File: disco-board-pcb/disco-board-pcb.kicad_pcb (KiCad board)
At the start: 2 copper layers, 57.2 x 82.6 mm, 6 parts, among them J101 Conn_02x32_Odd_Even, J102 Conn_02x32_Odd_Even, U101 MMA8653FCR1

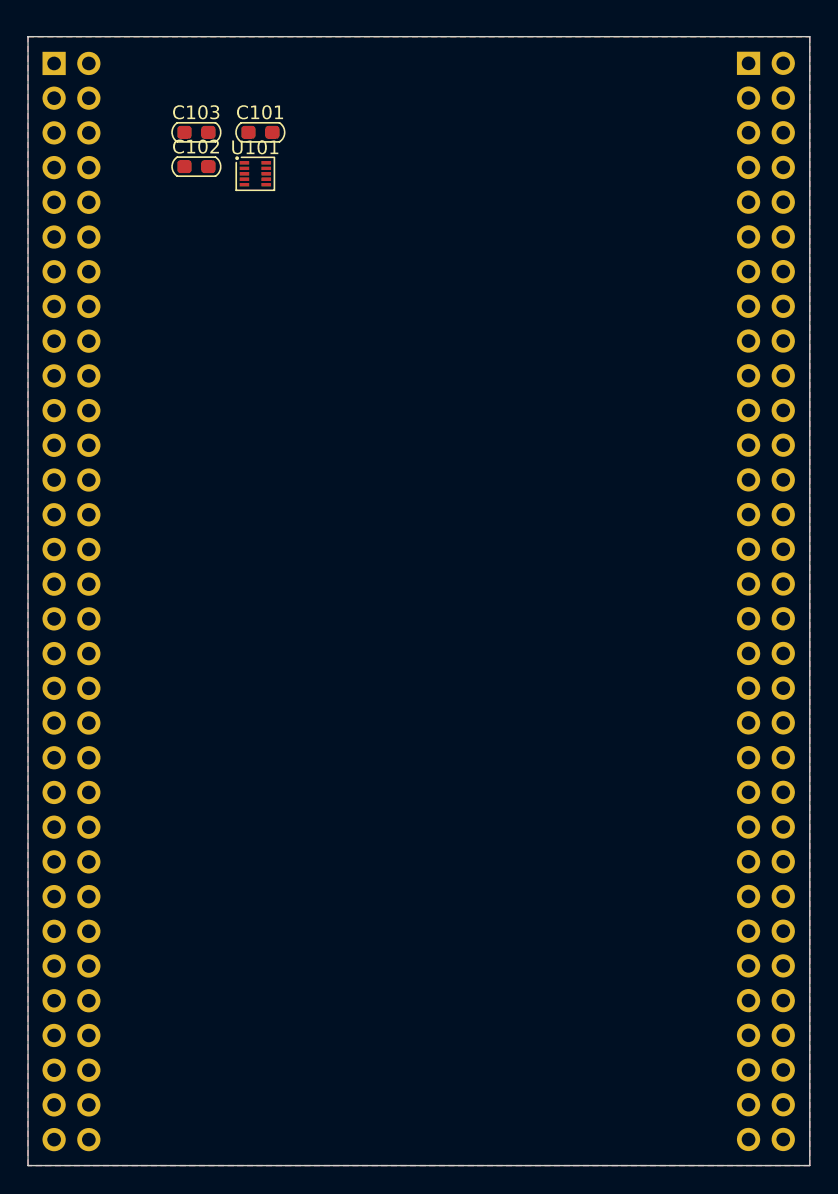
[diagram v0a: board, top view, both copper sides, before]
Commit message: Completing schematic and putting test points on PCB
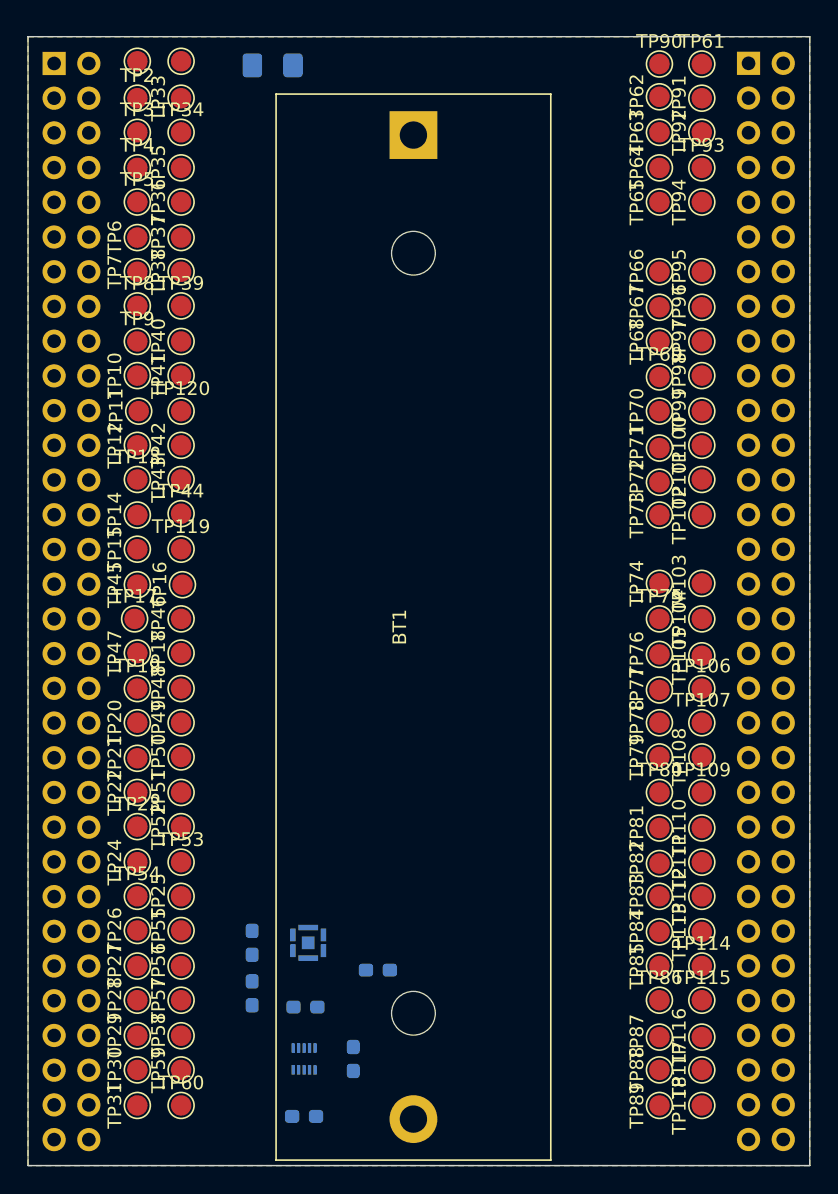
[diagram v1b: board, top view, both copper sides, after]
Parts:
- added BT1: Battery_Cell, Battery:BatteryHolder_MPD_BH-18650-PC2, F.Cu at (130.4, 65.8)
- added C2: LPS28DFWTR, local:LPS28DFWTR, B.Cu at (122.7, 124.9)
- added C5: 100nF, Capacitor_SMD_AKL:C_0603_1608Metric_Pad1.05x0.95mm, B.Cu at (127.8, 126.9)
- added F1: FUSE_SMD, Fuse_AKL:Fuse_1206_3216Metric_Pad1.42x1.75mm_BigPads, B.Cu at (120.1, 60.7)
- added R1: 10k, Resistor_SMD_AKL:R_0603_1608Metric_Pad1.05x0.95mm, B.Cu at (118.6, 124.9)
- added R2: 10k, Resistor_SMD_AKL:R_0603_1608Metric_Pad1.05x0.95mm, B.Cu at (118.6, 128.6)
- added TP1: TestPoint, TestPoint:TestPoint_Pad_D1.5mm, F.Cu at (110.2, 60.4)
- added TP10: TestPoint, TestPoint:TestPoint_Pad_D1.5mm, F.Cu at (110.2, 83.4)
- added TP100: TestPoint, TestPoint:TestPoint_Pad_D1.5mm, F.Cu at (151.5, 88.5)
- added TP101: TestPoint, TestPoint:TestPoint_Pad_D1.5mm, F.Cu at (151.5, 91.0)
- added TP102: TestPoint, TestPoint:TestPoint_Pad_D1.5mm, F.Cu at (151.5, 93.6)
- added TP103: TestPoint, TestPoint:TestPoint_Pad_D1.5mm, F.Cu at (151.5, 98.6)
- added TP104: TestPoint, TestPoint:TestPoint_Pad_D1.5mm, F.Cu at (151.5, 101.2)
- added TP105: TestPoint, TestPoint:TestPoint_Pad_D1.5mm, F.Cu at (151.5, 103.9)
- added TP106: TestPoint, TestPoint:TestPoint_Pad_D1.5mm, F.Cu at (151.5, 106.3)
- added TP107: TestPoint, TestPoint:TestPoint_Pad_D1.5mm, F.Cu at (151.5, 108.8)
- added TP108: TestPoint, TestPoint:TestPoint_Pad_D1.5mm, F.Cu at (151.5, 111.3)
- added TP109: TestPoint, TestPoint:TestPoint_Pad_D1.5mm, F.Cu at (151.5, 113.9)
- added TP11: TestPoint, TestPoint:TestPoint_Pad_D1.5mm, F.Cu at (110.3, 86.0)
- added TP110: TestPoint, TestPoint:TestPoint_Pad_D1.5mm, F.Cu at (151.5, 116.5)
- added TP111: TestPoint, TestPoint:TestPoint_Pad_D1.5mm, F.Cu at (151.5, 119.0)
- added TP112: TestPoint, TestPoint:TestPoint_Pad_D1.5mm, F.Cu at (151.5, 121.5)
- added TP113: TestPoint, TestPoint:TestPoint_Pad_D1.5mm, F.Cu at (151.5, 124.1)
- added TP114: TestPoint, TestPoint:TestPoint_Pad_D1.5mm, F.Cu at (151.5, 126.6)
- added TP115: TestPoint, TestPoint:TestPoint_Pad_D1.5mm, F.Cu at (151.5, 129.1)
- added TP116: TestPoint, TestPoint:TestPoint_Pad_D1.5mm, F.Cu at (151.5, 131.8)
- added TP117: TestPoint, TestPoint:TestPoint_Pad_D1.5mm, F.Cu at (151.5, 134.2)
- added TP118: TestPoint, TestPoint:TestPoint_Pad_D1.5mm, F.Cu at (151.5, 136.8)
- added TP119: TestPoint, TestPoint:TestPoint_Pad_D1.5mm, F.Cu at (113.4, 96.1)
- added TP12: TestPoint, TestPoint:TestPoint_Pad_D1.5mm, F.Cu at (110.2, 88.5)
- added TP120: TestPoint, TestPoint:TestPoint_Pad_D1.5mm, F.Cu at (113.4, 86.0)
- added TP13: TestPoint, TestPoint:TestPoint_Pad_D1.5mm, F.Cu at (110.2, 91.0)
- added TP14: TestPoint, TestPoint:TestPoint_Pad_D1.5mm, F.Cu at (110.2, 93.6)
- added TP15: TestPoint, TestPoint:TestPoint_Pad_D1.5mm, F.Cu at (110.2, 96.1)
- added TP16: TestPoint, TestPoint:TestPoint_Pad_D1.5mm, F.Cu at (113.5, 98.7)
- added TP17: TestPoint, TestPoint:TestPoint_Pad_D1.5mm, F.Cu at (110.0, 101.2)
- added TP18: TestPoint, TestPoint:TestPoint_Pad_D1.5mm, F.Cu at (113.4, 103.7)
- added TP19: TestPoint, TestPoint:TestPoint_Pad_D1.5mm, F.Cu at (110.2, 106.3)
- added TP2: TestPoint, TestPoint:TestPoint_Pad_D1.5mm, F.Cu at (110.2, 63.1)
- added TP20: TestPoint, TestPoint:TestPoint_Pad_D1.5mm, F.Cu at (110.2, 108.8)
- added TP21: TestPoint, TestPoint:TestPoint_Pad_D1.5mm, F.Cu at (110.2, 111.4)
- added TP22: TestPoint, TestPoint:TestPoint_Pad_D1.5mm, F.Cu at (110.2, 113.9)
- added TP23: TestPoint, TestPoint:TestPoint_Pad_D1.5mm, F.Cu at (110.2, 116.4)
- added TP24: TestPoint, TestPoint:TestPoint_Pad_D1.5mm, F.Cu at (110.2, 119.0)
- added TP25: TestPoint, TestPoint:TestPoint_Pad_D1.5mm, F.Cu at (113.4, 121.5)
- added TP26: TestPoint, TestPoint:TestPoint_Pad_D1.5mm, F.Cu at (110.2, 124.0)
- added TP27: TestPoint, TestPoint:TestPoint_Pad_D1.5mm, F.Cu at (110.2, 126.6)
- added TP28: TestPoint, TestPoint:TestPoint_Pad_D1.5mm, F.Cu at (110.2, 129.1)
- added TP29: TestPoint, TestPoint:TestPoint_Pad_D1.5mm, F.Cu at (110.2, 131.7)
- added TP3: TestPoint, TestPoint:TestPoint_Pad_D1.5mm, F.Cu at (110.2, 65.6)
- added TP30: TestPoint, TestPoint:TestPoint_Pad_D1.5mm, F.Cu at (110.2, 134.2)
- added TP31: TestPoint, TestPoint:TestPoint_Pad_D1.5mm, F.Cu at (110.2, 136.8)
- added TP32: TestPoint, TestPoint:TestPoint_Pad_D1.5mm, F.Cu at (113.4, 60.4)
- added TP33: TestPoint, TestPoint:TestPoint_Pad_D1.5mm, F.Cu at (113.4, 63.1)
- added TP34: TestPoint, TestPoint:TestPoint_Pad_D1.5mm, F.Cu at (113.4, 65.6)
- added TP35: TestPoint, TestPoint:TestPoint_Pad_D1.5mm, F.Cu at (113.4, 68.2)
- added TP36: TestPoint, TestPoint:TestPoint_Pad_D1.5mm, F.Cu at (113.4, 70.7)
- added TP37: TestPoint, TestPoint:TestPoint_Pad_D1.5mm, F.Cu at (113.4, 73.3)
- added TP38: TestPoint, TestPoint:TestPoint_Pad_D1.5mm, F.Cu at (113.4, 75.8)
- added TP39: TestPoint, TestPoint:TestPoint_Pad_D1.5mm, F.Cu at (113.4, 78.3)
- added TP4: TestPoint, TestPoint:TestPoint_Pad_D1.5mm, F.Cu at (110.2, 68.2)
- added TP40: TestPoint, TestPoint:TestPoint_Pad_D1.5mm, F.Cu at (113.4, 80.9)
- added TP41: TestPoint, TestPoint:TestPoint_Pad_D1.5mm, F.Cu at (113.4, 83.4)
- added TP42: TestPoint, TestPoint:TestPoint_Pad_D1.5mm, F.Cu at (113.4, 88.5)
- added TP43: TestPoint, TestPoint:TestPoint_Pad_D1.5mm, F.Cu at (113.4, 91.0)
- added TP44: TestPoint, TestPoint:TestPoint_Pad_D1.5mm, F.Cu at (113.4, 93.5)
- added TP45: TestPoint, TestPoint:TestPoint_Pad_D1.5mm, F.Cu at (110.2, 98.7)
- added TP46: TestPoint, TestPoint:TestPoint_Pad_D1.5mm, F.Cu at (113.4, 101.2)
- added TP47: TestPoint, TestPoint:TestPoint_Pad_D1.5mm, F.Cu at (110.2, 103.7)
- added TP48: TestPoint, TestPoint:TestPoint_Pad_D1.5mm, F.Cu at (113.4, 106.3)
- added TP49: TestPoint, TestPoint:TestPoint_Pad_D1.5mm, F.Cu at (113.4, 108.8)
- added TP5: TestPoint, TestPoint:TestPoint_Pad_D1.5mm, F.Cu at (110.2, 70.7)
- added TP50: TestPoint, TestPoint:TestPoint_Pad_D1.5mm, F.Cu at (113.4, 111.3)
- added TP51: TestPoint, TestPoint:TestPoint_Pad_D1.5mm, F.Cu at (113.4, 113.9)
- added TP52: TestPoint, TestPoint:TestPoint_Pad_D1.5mm, F.Cu at (113.4, 116.4)
- added TP53: TestPoint, TestPoint:TestPoint_Pad_D1.5mm, F.Cu at (113.4, 119.0)
- added TP54: TestPoint, TestPoint:TestPoint_Pad_D1.5mm, F.Cu at (110.2, 121.5)
- added TP55: TestPoint, TestPoint:TestPoint_Pad_D1.5mm, F.Cu at (113.4, 124.0)
- added TP56: TestPoint, TestPoint:TestPoint_Pad_D1.5mm, F.Cu at (113.4, 126.6)
- added TP57: TestPoint, TestPoint:TestPoint_Pad_D1.5mm, F.Cu at (113.4, 129.1)
- added TP58: TestPoint, TestPoint:TestPoint_Pad_D1.5mm, F.Cu at (113.4, 131.7)
- added TP59: TestPoint, TestPoint:TestPoint_Pad_D1.5mm, F.Cu at (113.4, 134.2)
- added TP6: TestPoint, TestPoint:TestPoint_Pad_D1.5mm, F.Cu at (110.2, 73.3)
- added TP60: TestPoint, TestPoint:TestPoint_Pad_D1.5mm, F.Cu at (113.4, 136.8)
- added TP61: TestPoint, TestPoint:TestPoint_Pad_D1.5mm, F.Cu at (151.5, 60.6)
- added TP62: TestPoint, TestPoint:TestPoint_Pad_D1.5mm, F.Cu at (148.4, 63.0)
- added TP63: TestPoint, TestPoint:TestPoint_Pad_D1.5mm, F.Cu at (148.4, 65.6)
- added TP64: TestPoint, TestPoint:TestPoint_Pad_D1.5mm, F.Cu at (148.4, 68.2)
- added TP65: TestPoint, TestPoint:TestPoint_Pad_D1.5mm, F.Cu at (148.4, 70.7)
- added TP66: TestPoint, TestPoint:TestPoint_Pad_D1.5mm, F.Cu at (148.4, 75.8)
- added TP67: TestPoint, TestPoint:TestPoint_Pad_D1.5mm, F.Cu at (148.4, 78.4)
- added TP68: TestPoint, TestPoint:TestPoint_Pad_D1.5mm, F.Cu at (148.4, 80.9)
- added TP69: TestPoint, TestPoint:TestPoint_Pad_D1.5mm, F.Cu at (148.4, 83.5)
- added TP7: TestPoint, TestPoint:TestPoint_Pad_D1.5mm, F.Cu at (110.2, 75.8)
- added TP70: TestPoint, TestPoint:TestPoint_Pad_D1.5mm, F.Cu at (148.4, 86.0)
- added TP71: TestPoint, TestPoint:TestPoint_Pad_D1.5mm, F.Cu at (148.4, 88.7)
- added TP72: TestPoint, TestPoint:TestPoint_Pad_D1.5mm, F.Cu at (148.4, 91.2)
- added TP73: TestPoint, TestPoint:TestPoint_Pad_D1.5mm, F.Cu at (148.4, 93.6)
- added TP74: TestPoint, TestPoint:TestPoint_Pad_D1.5mm, F.Cu at (148.4, 98.6)
- added TP75: TestPoint, TestPoint:TestPoint_Pad_D1.5mm, F.Cu at (148.4, 101.2)
- added TP76: TestPoint, TestPoint:TestPoint_Pad_D1.5mm, F.Cu at (148.4, 103.8)
- added TP77: TestPoint, TestPoint:TestPoint_Pad_D1.5mm, F.Cu at (148.4, 106.4)
- added TP78: TestPoint, TestPoint:TestPoint_Pad_D1.5mm, F.Cu at (148.4, 108.8)
- added TP79: TestPoint, TestPoint:TestPoint_Pad_D1.5mm, F.Cu at (148.4, 111.3)
- added TP8: TestPoint, TestPoint:TestPoint_Pad_D1.5mm, F.Cu at (110.2, 78.3)
- added TP80: TestPoint, TestPoint:TestPoint_Pad_D1.5mm, F.Cu at (148.4, 113.9)
- added TP81: TestPoint, TestPoint:TestPoint_Pad_D1.5mm, F.Cu at (148.4, 116.5)
- added TP82: TestPoint, TestPoint:TestPoint_Pad_D1.5mm, F.Cu at (148.4, 119.1)
- added TP83: TestPoint, TestPoint:TestPoint_Pad_D1.5mm, F.Cu at (148.4, 121.5)
- added TP84: TestPoint, TestPoint:TestPoint_Pad_D1.5mm, F.Cu at (148.4, 124.1)
- added TP85: TestPoint, TestPoint:TestPoint_Pad_D1.5mm, F.Cu at (148.4, 126.6)
- added TP86: TestPoint, TestPoint:TestPoint_Pad_D1.5mm, F.Cu at (148.4, 129.1)
- added TP87: TestPoint, TestPoint:TestPoint_Pad_D1.5mm, F.Cu at (148.4, 131.8)
- added TP88: TestPoint, TestPoint:TestPoint_Pad_D1.5mm, F.Cu at (148.4, 134.2)
- added TP89: TestPoint, TestPoint:TestPoint_Pad_D1.5mm, F.Cu at (148.4, 136.8)
- added TP9: TestPoint, TestPoint:TestPoint_Pad_D1.5mm, F.Cu at (110.2, 80.9)
- added TP90: TestPoint, TestPoint:TestPoint_Pad_D1.5mm, F.Cu at (148.4, 60.6)
- added TP91: TestPoint, TestPoint:TestPoint_Pad_D1.5mm, F.Cu at (151.5, 63.1)
- added TP92: TestPoint, TestPoint:TestPoint_Pad_D1.5mm, F.Cu at (151.5, 65.6)
- added TP93: TestPoint, TestPoint:TestPoint_Pad_D1.5mm, F.Cu at (151.5, 68.2)
- added TP94: TestPoint, TestPoint:TestPoint_Pad_D1.5mm, F.Cu at (151.5, 70.7)
- added TP95: TestPoint, TestPoint:TestPoint_Pad_D1.5mm, F.Cu at (151.5, 75.8)
- added TP96: TestPoint, TestPoint:TestPoint_Pad_D1.5mm, F.Cu at (151.5, 78.4)
- added TP97: TestPoint, TestPoint:TestPoint_Pad_D1.5mm, F.Cu at (151.5, 80.9)
- added TP98: TestPoint, TestPoint:TestPoint_Pad_D1.5mm, F.Cu at (151.5, 83.4)
- added TP99: TestPoint, TestPoint:TestPoint_Pad_D1.5mm, F.Cu at (151.5, 86.0)
- C1: renamed from C101; moved to B.Cu
- C3: renamed from C102; moved to B.Cu
- C4: renamed from C103; moved to B.Cu
- U1: renamed from U101; moved to B.Cu
- moved C3 69.9 mm to (122.4, 137.6)
- moved C1 68.1 mm to (126.0, 133.4), turned to -90 degrees
- moved U1 64.9 mm to (122.4, 133.4), turned to -90 degrees
- moved C4 64.5 mm to (122.5, 129.6)
- renumbered J101 to J1, J102 to J2
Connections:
- J1 pad 10: unconnected-(J101-Pad10) -> Net-(J1-Pad10)
- J1 pad 11: unconnected-(J101-Pad11) -> /GPIO_PE6
- J1 pad 12: unconnected-(J101-Pad12) -> /GPIO_PC13
- J1 pad 13: unconnected-(J101-Pad13) -> /GPIO_PE4
- J1 pad 14: unconnected-(J101-Pad14) -> /GPIO_PE5
- J1 pad 15: unconnected-(J101-Pad15) -> /GPIO_PE2
- J1 pad 16: unconnected-(J101-Pad16) -> /GPIO_PE3
- J1 pad 17: unconnected-(J101-Pad17) -> Net-(J1-Pad17)
- J1 pad 18: unconnected-(J101-Pad18) -> Net-(J1-Pad18)
- J1 pad 19: unconnected-(J101-Pad19) -> Net-(J1-Pad19)
- J1 pad 20: unconnected-(J101-Pad20) -> Net-(J1-Pad20)
- J1 pad 21: unconnected-(J101-Pad21) -> Net-(J1-Pad21)
- J1 pad 23: unconnected-(J101-Pad23) -> Net-(J1-Pad23)
- J1 pad 24: unconnected-(J101-Pad24) -> /GPIO_PB7
- J1 pad 25: unconnected-(J101-Pad25) -> /GPIO_PB4
- J1 pad 26: unconnected-(J101-Pad26) -> Net-(J1-Pad26)
- J1 pad 27: unconnected-(J101-Pad27) -> Net-(J1-Pad27)
- J1 pad 28: unconnected-(J101-Pad28) -> Net-(J1-Pad28)
- J1 pad 29: unconnected-(J101-Pad29) -> Net-(J1-Pad29)
- J1 pad 3: unconnected-(J101-Pad3) -> Net-(J1-Pad3)
- J1 pad 30: unconnected-(J101-Pad30) -> Net-(J1-Pad30)
- J1 pad 31: unconnected-(J101-Pad31) -> Net-(J1-Pad31)
- J1 pad 32: unconnected-(J101-Pad32) -> Net-(J1-Pad32)
- J1 pad 33: unconnected-(J101-Pad33) -> /GPIO_PG9
- J1 pad 34: unconnected-(J101-Pad34) -> Net-(J1-Pad34)
- J1 pad 35: unconnected-(J101-Pad35) -> /GPIO_PD7
- J1 pad 36: unconnected-(J101-Pad36) -> Net-(J1-Pad36)
- J1 pad 37: unconnected-(J101-Pad37) -> /GPIO_PD5
- J1 pad 38: unconnected-(J101-Pad38) -> /GPIO_PD4
- J1 pad 39: unconnected-(J101-Pad39) -> Net-(J1-Pad39)
- J1 pad 4: unconnected-(J101-Pad4) -> Net-(J1-Pad4)
- J1 pad 40: unconnected-(J101-Pad40) -> /GPIO_PD2
- J1 pad 41: unconnected-(J101-Pad41) -> Net-(J1-Pad41)
- J1 pad 42: unconnected-(J101-Pad42) -> Net-(J1-Pad42)
- J1 pad 43: unconnected-(J101-Pad43) -> /GPIO_PC12
- J1 pad 44: unconnected-(J101-Pad44) -> /GPIO_PC11
- J1 pad 45: unconnected-(J101-Pad45) -> Net-(J1-Pad45)
- J1 pad 46: unconnected-(J101-Pad46) -> Net-(J1-Pad46)
- J1 pad 47: unconnected-(J101-Pad47) -> Net-(J1-Pad47)
- J1 pad 48: unconnected-(J101-Pad48) -> Net-(J1-Pad48)
- J1 pad 49: unconnected-(J101-Pad49) -> Net-(J1-Pad49)
- J1 pad 5: unconnected-(J101-Pad5) -> Net-(J1-Pad5)
- J1 pad 50: unconnected-(J101-Pad50) -> Net-(J1-Pad50)
- J1 pad 51: unconnected-(J101-Pad51) -> Net-(J1-Pad51)
- J1 pad 52: unconnected-(J101-Pad52) -> Net-(J1-Pad52)
- J1 pad 55: unconnected-(J101-Pad55) -> /GPIO_PC8
- J1 pad 56: unconnected-(J101-Pad56) -> Net-(J1-Pad56)
- J1 pad 57: unconnected-(J101-Pad57) -> Net-(J1-Pad57)
- J1 pad 58: unconnected-(J101-Pad58) -> Net-(J1-Pad58)
- J1 pad 59: unconnected-(J101-Pad59) -> Net-(J1-Pad59)
- J1 pad 6: unconnected-(J101-Pad6) -> Net-(J1-Pad6)
- J1 pad 60: unconnected-(J101-Pad60) -> Net-(J1-Pad60)
- J1 pad 61: unconnected-(J101-Pad61) -> Net-(J1-Pad61)
- J1 pad 62: unconnected-(J101-Pad62) -> Net-(J1-Pad62)
- J1 pad 7: unconnected-(J101-Pad7) -> Net-(J1-Pad7)
- J1 pad 8: unconnected-(J101-Pad8) -> Net-(J1-Pad8)
- J1 pad 9: unconnected-(J101-Pad9) -> Net-(J1-Pad9)
- J2 pad 10: unconnected-(J102-Pad10) -> Net-(J2-Pad10)
- J2 pad 13: unconnected-(J102-Pad13) -> Net-(J2-Pad13)
- J2 pad 14: unconnected-(J102-Pad14) -> Net-(J2-Pad14)
- J2 pad 15: unconnected-(J102-Pad15) -> Net-(J2-Pad15)
- J2 pad 16: unconnected-(J102-Pad16) -> Net-(J2-Pad16)
- J2 pad 17: unconnected-(J102-Pad17) -> Net-(J2-Pad17)
- J2 pad 18: unconnected-(J102-Pad18) -> Net-(J2-Pad18)
- J2 pad 19: unconnected-(J102-Pad19) -> Net-(J2-Pad19)
- J2 pad 20: unconnected-(J102-Pad20) -> Net-(J2-Pad20)
- J2 pad 21: unconnected-(J102-Pad21) -> /GPIO_PA5
- J2 pad 22: unconnected-(J102-Pad22) -> Net-(J2-Pad22)
- J2 pad 24: unconnected-(J102-Pad24) -> Net-(J2-Pad24)
- J2 pad 25: unconnected-(J102-Pad25) -> Net-(J2-Pad25)
- J2 pad 26: unconnected-(J102-Pad26) -> Net-(J2-Pad26)
- J2 pad 27: unconnected-(J102-Pad27) -> Net-(J2-Pad27)
- J2 pad 28: unconnected-(J102-Pad28) -> Net-(J2-Pad28)
- J2 pad 3: unconnected-(J102-Pad3) -> /GPIO_PF6
- J2 pad 31: unconnected-(J102-Pad31) -> Net-(J2-Pad31)
- J2 pad 32: unconnected-(J102-Pad32) -> Net-(J2-Pad32)
- J2 pad 33: unconnected-(J102-Pad33) -> Net-(J2-Pad33)
- J2 pad 34: unconnected-(J102-Pad34) -> Net-(J2-Pad34)
- J2 pad 35: unconnected-(J102-Pad35) -> Net-(J2-Pad35)
- J2 pad 36: unconnected-(J102-Pad36) -> Net-(J2-Pad36)
- J2 pad 37: unconnected-(J102-Pad37) -> Net-(J2-Pad37)
- J2 pad 38: unconnected-(J102-Pad38) -> Net-(J2-Pad38)
- J2 pad 39: unconnected-(J102-Pad39) -> Net-(J2-Pad39)
- J2 pad 4: unconnected-(J102-Pad4) -> Net-(J2-Pad4)
- J2 pad 40: unconnected-(J102-Pad40) -> Net-(J2-Pad40)
- J2 pad 41: unconnected-(J102-Pad41) -> Net-(J2-Pad41)
- J2 pad 42: unconnected-(J102-Pad42) -> Net-(J2-Pad42)
- J2 pad 43: unconnected-(J102-Pad43) -> Net-(J2-Pad43)
- J2 pad 44: unconnected-(J102-Pad44) -> Net-(J2-Pad44)
- J2 pad 45: unconnected-(J102-Pad45) -> Net-(J2-Pad45)
- J2 pad 46: unconnected-(J102-Pad46) -> Net-(J2-Pad46)
- J2 pad 47: unconnected-(J102-Pad47) -> Net-(J2-Pad47)
- J2 pad 48: unconnected-(J102-Pad48) -> Net-(J2-Pad48)
- J2 pad 49: unconnected-(J102-Pad49) -> Net-(J2-Pad49)
- J2 pad 5: unconnected-(J102-Pad5) -> Net-(J2-Pad5)
- J2 pad 50: unconnected-(J102-Pad50) -> Net-(J2-Pad50)
- J2 pad 51: unconnected-(J102-Pad51) -> Net-(J2-Pad51)
- J2 pad 52: unconnected-(J102-Pad52) -> Net-(J2-Pad52)
- J2 pad 53: unconnected-(J102-Pad53) -> Net-(J2-Pad53)
- J2 pad 54: unconnected-(J102-Pad54) -> Net-(J2-Pad54)
- J2 pad 55: unconnected-(J102-Pad55) -> Net-(J2-Pad55)
- J2 pad 56: unconnected-(J102-Pad56) -> Net-(J2-Pad56)
- J2 pad 57: unconnected-(J102-Pad57) -> Net-(J2-Pad57)
- J2 pad 58: unconnected-(J102-Pad58) -> Net-(J2-Pad58)
- J2 pad 59: unconnected-(J102-Pad59) -> Net-(J2-Pad59)
- J2 pad 6: unconnected-(J102-Pad6) -> Net-(J2-Pad6)
- J2 pad 60: unconnected-(J102-Pad60) -> Net-(J2-Pad60)
- J2 pad 61: unconnected-(J102-Pad61) -> /GPIO_PG3
- J2 pad 62: unconnected-(J102-Pad62) -> /GPIO_PG2
- J2 pad 7: unconnected-(J102-Pad7) -> Net-(J2-Pad7)
- J2 pad 8: unconnected-(J102-Pad8) -> Net-(J2-Pad8)
- J2 pad 9: unconnected-(J102-Pad9) -> Net-(J2-Pad9)

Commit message: Started routing
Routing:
- net +5V: track 0.00 -> 9.36 mm
- net VDD: track 0.00 -> 7.68 mm
- net Net-(J1-Pad20): track 0.00 -> 7.67 mm
- net /GPIO_PC13: track 0.00 -> 7.66 mm
- net Net-(J1-Pad18): track 0.00 -> 7.65 mm
- net Net-(J1-Pad8): track 0.00 -> 7.65 mm
- net /GPIO_PE3: track 0.00 -> 7.64 mm
- net /GPIO_PE5: track 0.00 -> 7.64 mm
- net Net-(J1-Pad4): track 0.00 -> 7.64 mm
- net Net-(J1-Pad10): track 0.00 -> 7.63 mm
- net Net-(J1-Pad6): track 0.00 -> 7.62 mm
- net Net-(J1-Pad21): track 0.00 -> 7.18 mm
- net Net-(J1-Pad3): track 0.00 -> 7.13 mm
- net /GPIO_PE6: track 0.00 -> 7.08 mm
- net Net-(J1-Pad7): track 0.00 -> 7.07 mm
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
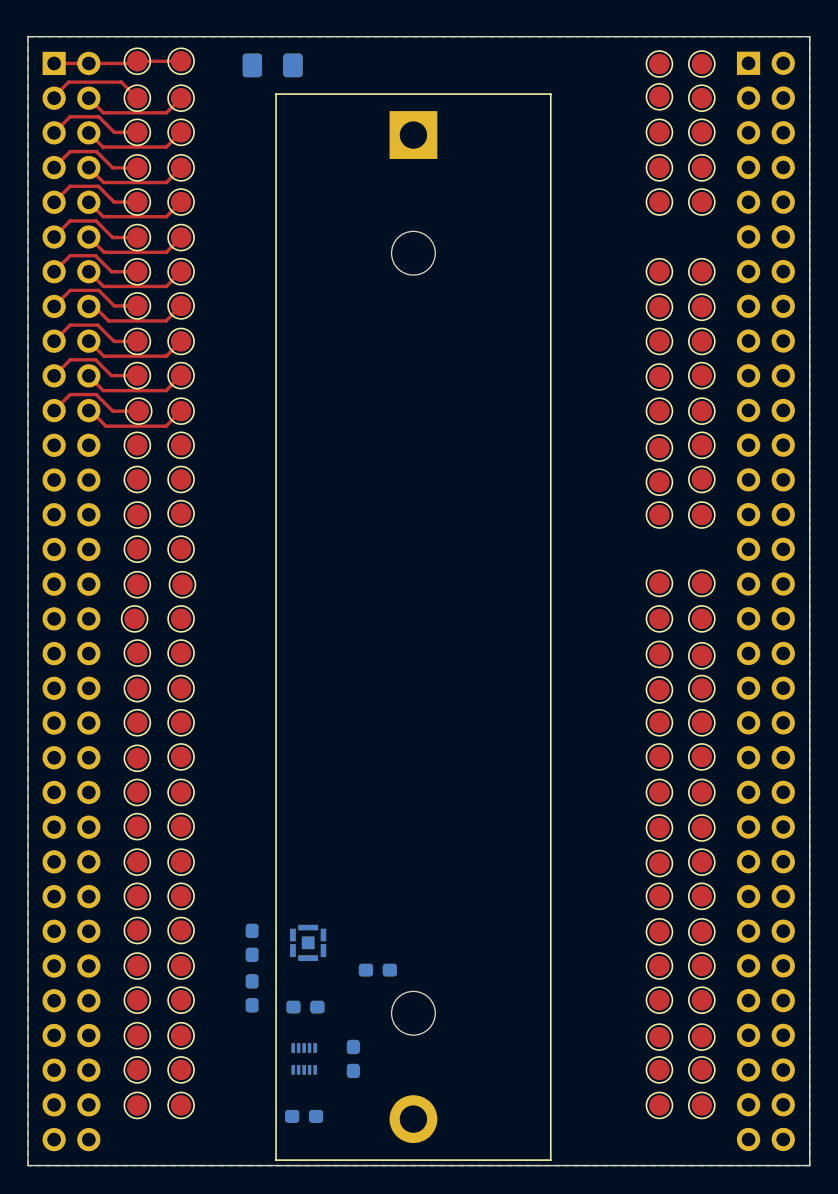
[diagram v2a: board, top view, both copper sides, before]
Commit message: Routed all test points
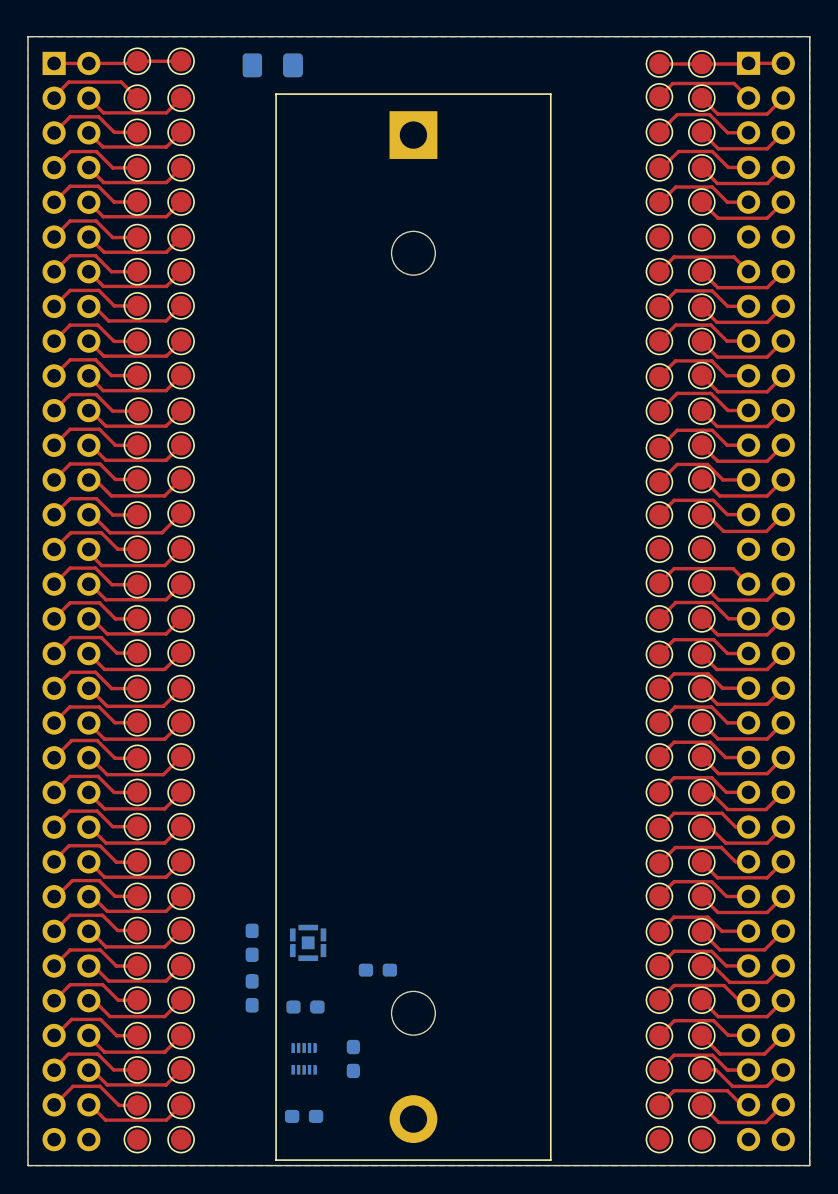
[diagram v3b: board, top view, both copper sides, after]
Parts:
- added TP121: TestPoint, TestPoint:TestPoint_Pad_D1.5mm, F.Cu at (151.5, 73.3)
- added TP122: TestPoint, TestPoint:TestPoint_Pad_D1.5mm, F.Cu at (148.4, 139.3)
- added TP123: TestPoint, TestPoint:TestPoint_Pad_D1.5mm, F.Cu at (148.4, 73.3)
- added TP124: TestPoint, TestPoint:TestPoint_Pad_D1.5mm, F.Cu at (151.5, 139.3)
- added TP125: TestPoint, TestPoint:TestPoint_Pad_D1.5mm, F.Cu at (148.4, 96.1)
- added TP126: TestPoint, TestPoint:TestPoint_Pad_D1.5mm, F.Cu at (113.4, 139.3)
- added TP127: TestPoint, TestPoint:TestPoint_Pad_D1.5mm, F.Cu at (110.2, 139.3)
- added TP128: TestPoint, TestPoint:TestPoint_Pad_D1.5mm, F.Cu at (151.5, 96.1)
- moved TP16 3.30 mm to (110.2, 98.7)
- moved TP18 3.20 mm to (110.2, 103.7)
- moved TP25 3.20 mm to (110.2, 121.5)
- moved TP45 3.20 mm to (113.4, 98.7)
- moved TP47 3.20 mm to (113.4, 103.7)
- moved TP54 3.20 mm to (113.4, 121.5)
- moved TP17 0.20 mm to (110.2, 101.2)
- moved TP116 0.10 mm to (151.5, 131.7)
- moved TP87 0.10 mm to (148.4, 131.7)
- moved TP105 0.10 mm to (151.5, 103.8)
- moved TP77 0.10 mm to (148.4, 106.3)
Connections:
- U1 pad 7: unconnected-(U1-Pad7) -> GND
- U1 pad 8: unconnected-(U1-Pad8) -> +3V0
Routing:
- net +3V0: track 0.00 -> 9.08 mm
- net Net-(J1-Pad28): track 0.00 -> 7.88 mm
- net Net-(J1-Pad30): track 0.00 -> 7.87 mm
- net /GPIO_PD4: track 0.00 -> 7.84 mm
- net Net-(J1-Pad42): track 0.00 -> 7.80 mm
- net Net-(J1-Pad58): track 0.00 -> 7.79 mm
- net /GPIO_PC11: track 0.00 -> 7.77 mm
- net /GPIO_PD2: track 0.00 -> 7.75 mm
- net Net-(J1-Pad36): track 0.00 -> 7.73 mm
- net Net-(J1-Pad56): track 0.00 -> 7.73 mm
- net Net-(J1-Pad26): track 0.00 -> 7.73 mm
- net Net-(J1-Pad46): track 0.00 -> 7.73 mm
- net Net-(J1-Pad52): track 0.00 -> 7.72 mm
- net Net-(J1-Pad32): track 0.00 -> 7.68 mm
- net Net-(J1-Pad48): track 0.00 -> 7.67 mm
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
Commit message: Completed routing the board
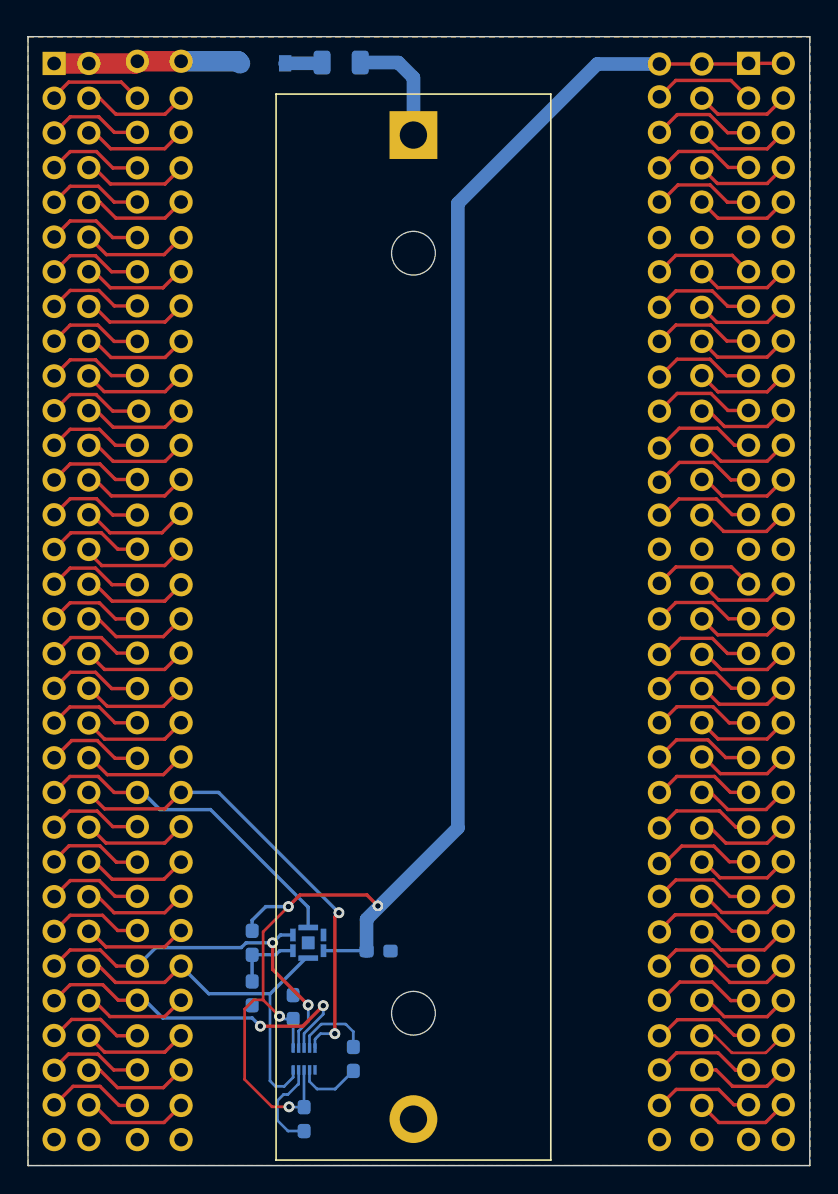
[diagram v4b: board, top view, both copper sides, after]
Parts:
- added D1: 1N4148W, Diode_SMD:D_SOD-123, B.Cu at (119.4, 60.5)
- C2: value LPS28DFWTR -> CCLGA7_LPS28DFWTR_STM
- F1: value FUSE_SMD -> Fuse_Small; footprint Fuse_AKL:Fuse_1206_3216Metric_Pad1.42x1.75mm_BigPads -> Fuse_AKL:Fuse_1206_3216Metric
- TP1, TP10, TP100, TP101, TP102, TP103, TP104, TP105, TP106, TP107, TP108, TP109, TP11, TP110, TP111, TP112, TP113, TP114, TP115, TP116, TP117, TP118, TP119, TP12, TP120, TP121, TP122, TP123, TP124, TP125, TP126, TP127, TP128, TP13, TP14, TP15, TP16, TP17, TP18, TP19, TP2, TP20, TP21, TP22, TP23, TP24, TP25, TP26, TP27, TP28, TP29, TP3, TP30, TP31, TP32, TP33, TP34, TP35, TP36, TP37, TP38, TP39, TP4, TP40, TP41, TP42, TP43, TP44, TP45, TP46, TP47, TP48, TP49, TP5, TP50, TP51, TP52, TP53, TP54, TP55, TP56, TP57, TP58, TP59, TP6, TP60, TP61, TP62, TP63, TP64, TP65, TP66, TP67, TP68, TP69, TP7, TP70, TP71, TP72, TP73, TP74, TP75, TP76, TP77, TP78, TP79, TP8, TP80, TP81, TP82, TP83, TP84, TP85, TP86, TP87, TP88, TP89, TP9, TP90, TP91, TP92, TP93, TP94, TP95, TP96, TP97, TP98, TP99: footprint TestPoint:TestPoint_Pad_D1.5mm -> local:PinHeader_1x1_testpad
- moved F1 5.02 mm to (125.1, 60.5)
- moved C5 1.40 mm to (127.8, 125.5)
- moved C4 0.90 mm to (121.6, 129.6), turned to 90 degrees
- moved C3 0.20 mm to (122.4, 137.8), turned to -90 degrees
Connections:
- C2 pad 4: /INT_DRDY -> /GPIO_PC12
- F1 pad 2: +5V -> Net-(D1-Pad2)
- J1 pad 44: /GPIO_PC11 -> /AINT2
- J1 pad 55: /GPIO_PC8 -> /AINT1
- TP28 pad 1: /GPIO_PC8 -> /AINT1
- TP51 pad 1: /GPIO_PC11 -> /AINT2
- U1 pad 3: unconnected-(U1-Pad3) -> /AINT1
- U1 pad 5: unconnected-(U1-Pad5) -> /AINT2
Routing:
- net +3V0: track 9.08 -> 127.0 mm, vias 0 -> 4
- net /AINT2: track 0.00 -> 34.2 mm, vias 0 -> 2
- net /AINT1: track 0.00 -> 25.7 mm, vias 0 -> 2
- net /SCL: track 7.06 -> 28.5 mm, vias 0 -> 2
- net /SDA: track 7.66 -> 28.0 mm
- net /GPIO_PC12: track 7.07 -> 24.5 mm
- net GND: track 0.00 -> 11.6 mm
- net Net-(BT1-Pad1): track 0.00 -> 8.55 mm
- net /GPIO_PC11: track 7.77 -> 0.00 mm
- net /GPIO_PC8: track 7.05 -> 0.00 mm
- net Net-(C1-Pad1): track 0.00 -> 5.80 mm
- net Net-(C2-Pad2): track 0.00 -> 5.06 mm
- net +5V: track 9.36 -> 13.7 mm
- net Net-(D1-Pad2): track 0.00 -> 2.72 mm
